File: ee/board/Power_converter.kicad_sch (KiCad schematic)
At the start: 40 parts, among them U4 AP62301Z6-7, U5 AP62301Z6-7, U6 AP62301Z6-7, U8 AP62301Z6-7

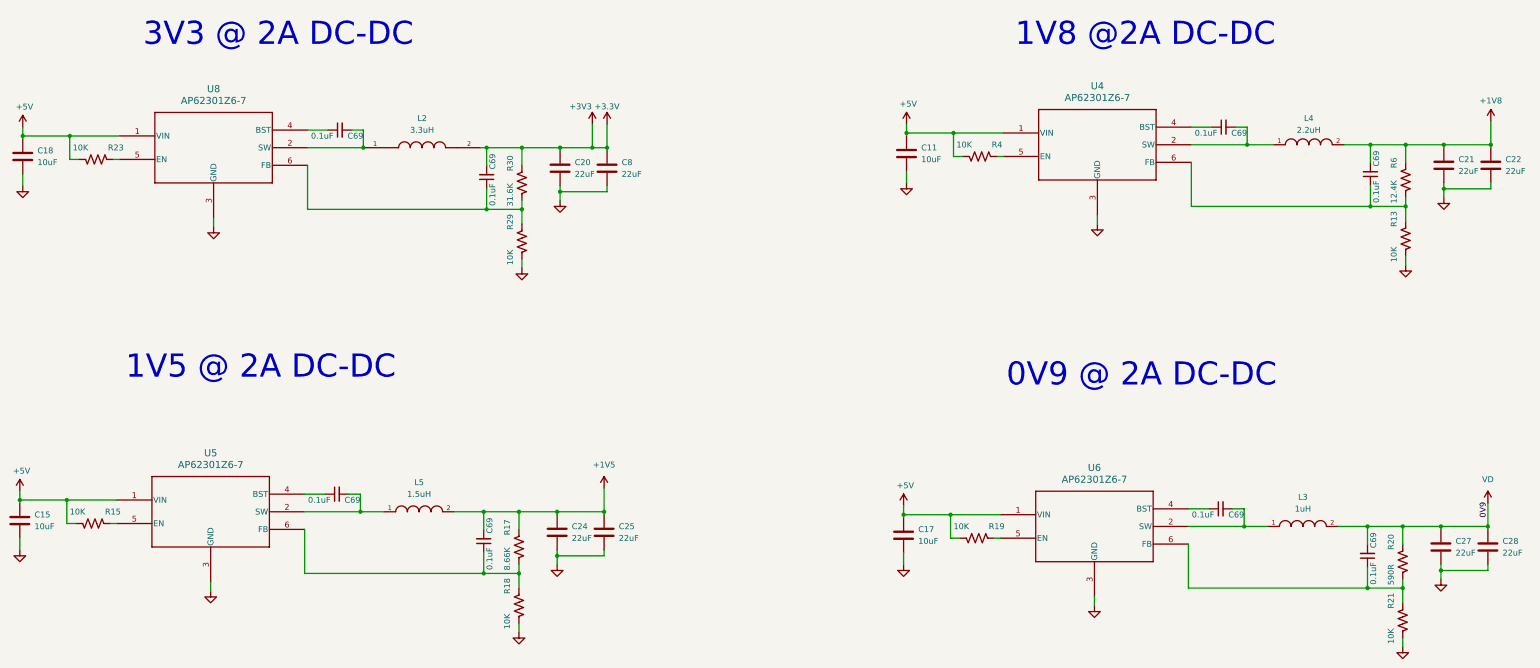
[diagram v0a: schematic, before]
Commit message: Added the footprints into the design.
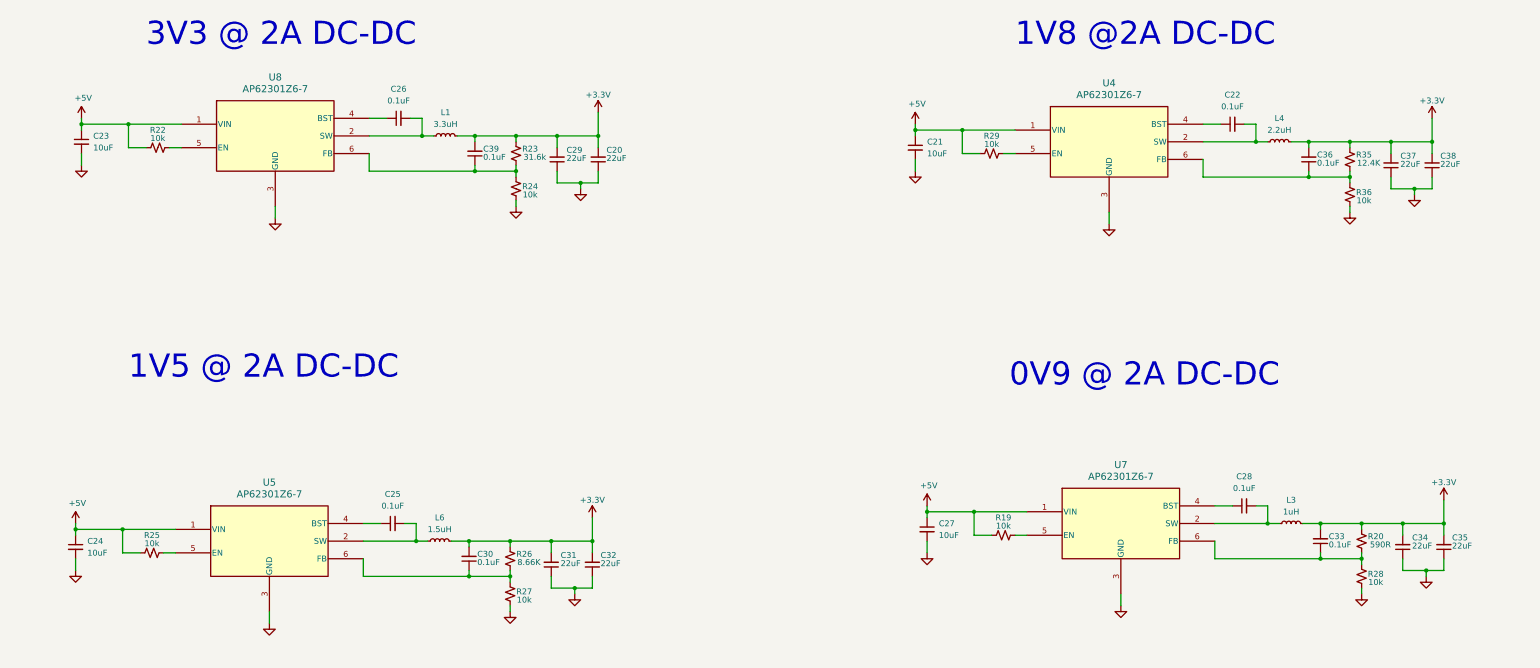
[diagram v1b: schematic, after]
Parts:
- removed C11, C15, C17, C18: 10uF, Capacitor_SMD:C_0805_2012Metric, symbol Device:C
- removed C20, C21, C22, C24, C25, C27, C28, C8: 22uF, Capacitor_SMD:C_0805_2012Metric, symbol Device:C
- removed C69 (x7): 16V 0.1uF X7R 0402, Capacitor_SMD:C_0402_1005Metric, symbol Device:C_Small
- removed L2: 3.3uH, 3.3uH:IND_1235AS-H-3R3M=P3, symbol 3.3uH:1235AS-H-3R3M=P3
- removed L3: 1uH, 74479276210C:IND_WE-PMCI_0806_WRE, symbol DFE252010P-1R5M_P2:DFE252010P-1R5M=P2
- removed L4: 2.2uH, DFE201612P_2R2M_P2:INDC2016X120N, symbol DFE201612P-2R2M_P2:DFE201612P-2R2M=P2
- removed L5: 1.5uH, DFE252010P_1R5M_P2:INDC2520X100N, symbol DFE252010P-1R5M_P2:DFE252010P-1R5M=P2
- removed R13, R15, R18, R19, R21, R23, R29, R4: 10K, Resistor_SMD:R_0603_1608Metric, symbol Device:R_US
- removed R17: 8.66K, Resistor_SMD:R_0603_1608Metric, symbol Device:R_US
- removed R20: 590R, Resistor_SMD:R_0603_1608Metric, symbol Device:R_US
- removed R30: 31.6K, Resistor_SMD:R_0603_1608Metric, symbol Device:R_US
- removed R6: 12.4K, Resistor_SMD:R_0603_1608Metric, symbol Device:R_US
- removed U6: AP62301Z6-7, AP62301Z6-7:SOT563-Z6_1_DIO, symbol AP62301Z6-7:AP62301Z6-7
- added C20, C29, C31, C32, C34, C35, C37, C38: 22uF, Capacitor_SMD:C_0603_1608Metric, symbol Device:C_Small
- added C21, C23, C24, C27: 10uF, Capacitor_SMD:C_0603_1608Metric, symbol Device:C_Small
- added C22, C25, C26, C28, C30, C33, C36: 0.1uF, Capacitor_SMD:C_0402_1005Metric, symbol Device:C_Small
- added L1: 3.3uH, Capacitor_SMD:C_0402_1005Metric, symbol Device:L_Small
- added L3: 1uH, symbol Device:L_Small
- added L4: 2.2uH, symbol Device:L_Small
- added L6: 1.5uH, symbol Device:L_Small
- added R19, R22, R24, R25, R27, R28, R29, R36: 10k, Resistor_SMD:R_0402_1005Metric, symbol Device:R_Small_US
- added R20: 590R, Resistor_SMD:R_0402_1005Metric, symbol Device:R_Small_US
- added R23: 31.6k, Resistor_SMD:R_0402_1005Metric, symbol Device:R_Small_US
- added R26: 8.66K, Resistor_SMD:R_0402_1005Metric, symbol Device:R_Small_US
- added R35: 12.4K, Resistor_SMD:R_0402_1005Metric, symbol Device:R_Small_US
- added U7: AP62301Z6-7, AP62301Z6-7:SOT563-Z6_1_DIO, symbol AP62301Z6-7:AP62301Z6-7
- C39: renamed from C69; value 16V 0.1uF X7R 0402 -> 0.1uF; Capacitance 0.1uF -> (none)
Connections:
- net +3.3V: now also C20.2, C29.2, C30.2, C31.2, C32.2, C33.2, C34.2, C35.2, C36.2, C37.2, C38.2, L1.2, L3.2, L4.2, L6.2, R20.2, R23.2, R26.2, R35.2
- net +5V: now also C21.1, C23.1, C24.1, C27.1, R19.1, R22.1, R25.1, R29.1, U7.1 (VIN)
- net GND: now also C20.1, C21.2, C23.2, C24.2, C27.2, C29.1, C31.1, C32.1, C34.1, C35.1, C37.1, C38.1, R24.1, R27.1, R28.1, R36.1, U7.3 (GND)
- net at U5.2 (SW): now also C25.2, L6.1
- net at U5.4 (BST): now also C25.1
- net at U5.5 (EN): now also R25.2
- net at U5.6 (FB): now also C30.1, R26.1, R27.2
- net at C39.1, U8.6 (FB): now also R23.1, R24.2
- net at U8.5 (EN): now also R22.2
- net at U4.2 (SW): now also C22.2, L4.1
- net at U4.4 (BST): now also C22.1
- net at U4.5 (EN): now also R29.2
- net at U4.6 (FB): now also C36.1, R35.1, R36.2
- net at U8.2 (SW): now also C26.2, L1.1
- net at U8.4 (BST): now also C26.1
- new net: R19.2, U7.5 (EN)
- new net: C33.1, R20.1, R28.2, U7.6 (FB)
- new net: C28.1, U7.4 (BST)
- new net: C28.2, L3.1, U7.2 (SW)
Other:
- moved on the sheet: C39
